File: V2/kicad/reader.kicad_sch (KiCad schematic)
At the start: 88 parts, among them SW1 SW_Rezistance, SW2 SW_src, U1 STM32H523CET6, U2 MAX98357AETE+T, U3 MLD-TF PUSH-H18, U4 TCAN1057AVDRQ1, U5 ESD2CAN24-ES, U6 RJ-064-1, U7 MCP16301Hx-xCH, Y1 16MHz

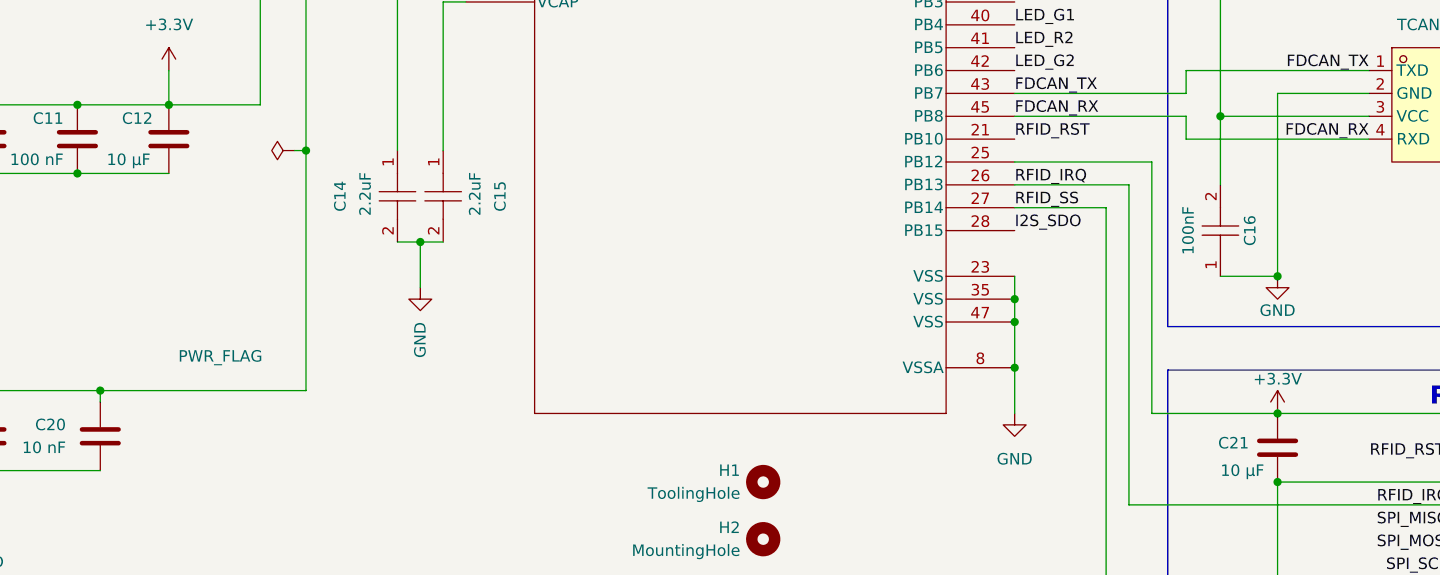
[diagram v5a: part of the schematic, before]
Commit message: small changes... stm32 pins in cubemx set based on schematic.
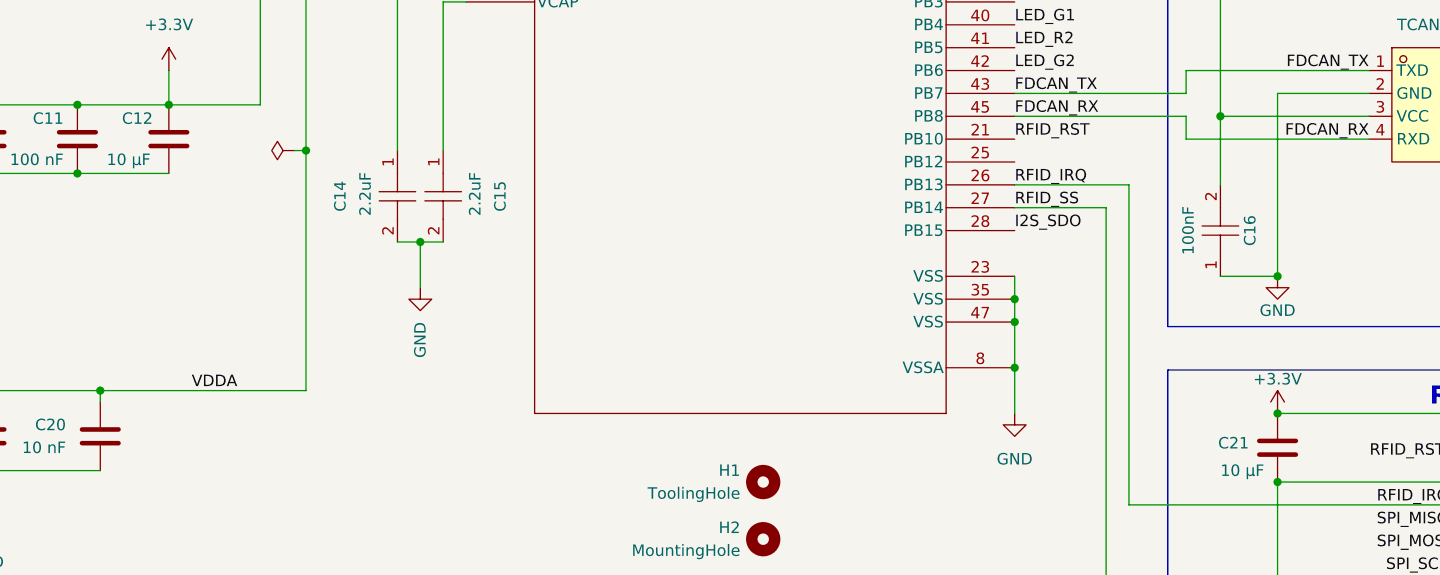
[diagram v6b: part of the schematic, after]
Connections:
- net +3.3V: no longer U1.25 (PB12)
- net VDDA: now reaches C19.1, C20.1, FB1.1, U1.9 (VDDA)
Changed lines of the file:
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@@
 	(wire
 		(pts
-			(xy 180.34 132.08) (xy 180.34 160.02)
-		)
-		(stroke
-			(width 0)
-			(type default)
-		)
-	)
-	(wire
-		(pts
 			(xy 91.44 50.8) (xy 91.44 38.1)
 		)
@@
 	(wire
 		(pts
-			(xy 165.1 132.08) (xy 180.34 132.08)
-		)
-		(stroke
-			(width 0)
-			(type default)
-		)
-	)
-	(wire
-		(pts
 			(xy 165.1 137.16) (xy 175.26 137.16)
 		)
@@
 	(wire
 		(pts
-			(xy 180.34 160.02) (xy 194.31 160.02)
-		)
-		(stroke
-			(width 0)
-			(type default)
-		)
-	)
-	(wire
-		(pts
 			(xy 176.53 255.27) (xy 176.53 252.73)
 		)
@@
 		)
 	)
+	(label "VDDA"
+		(at 73.66 157.48 0)
+		(effects
+			(font
+				(size 1.27 1.27)
+			)
+			(justify left bottom)
+		)
+	)
 	(label "RFID_IRQ"
 		(at 165.1 134.62 0)
@@
 		(property "Value" "PWR_FLAG"
 			(at 81.534 153.67 90)
+			(hide yes)
 			(show_name no)
 			(do_not_autoplace no)
